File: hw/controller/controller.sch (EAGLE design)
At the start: 74 parts, among them J1 JST-PH3SMT_VERT, J2 JST-PH3SMT_VERT, Q1 TPN1R603PL, Q2 TPN1R603PL, Q3 TPN1R603PL, Q4 TPN1R603PL, Q5 TPN1R603PL, Q6 TPN1R603PL, U1 STM32F4R_64PIN, U2 DRV8323RS, U3 AS5147, U4 MAX13431E, X1 8.0MHz

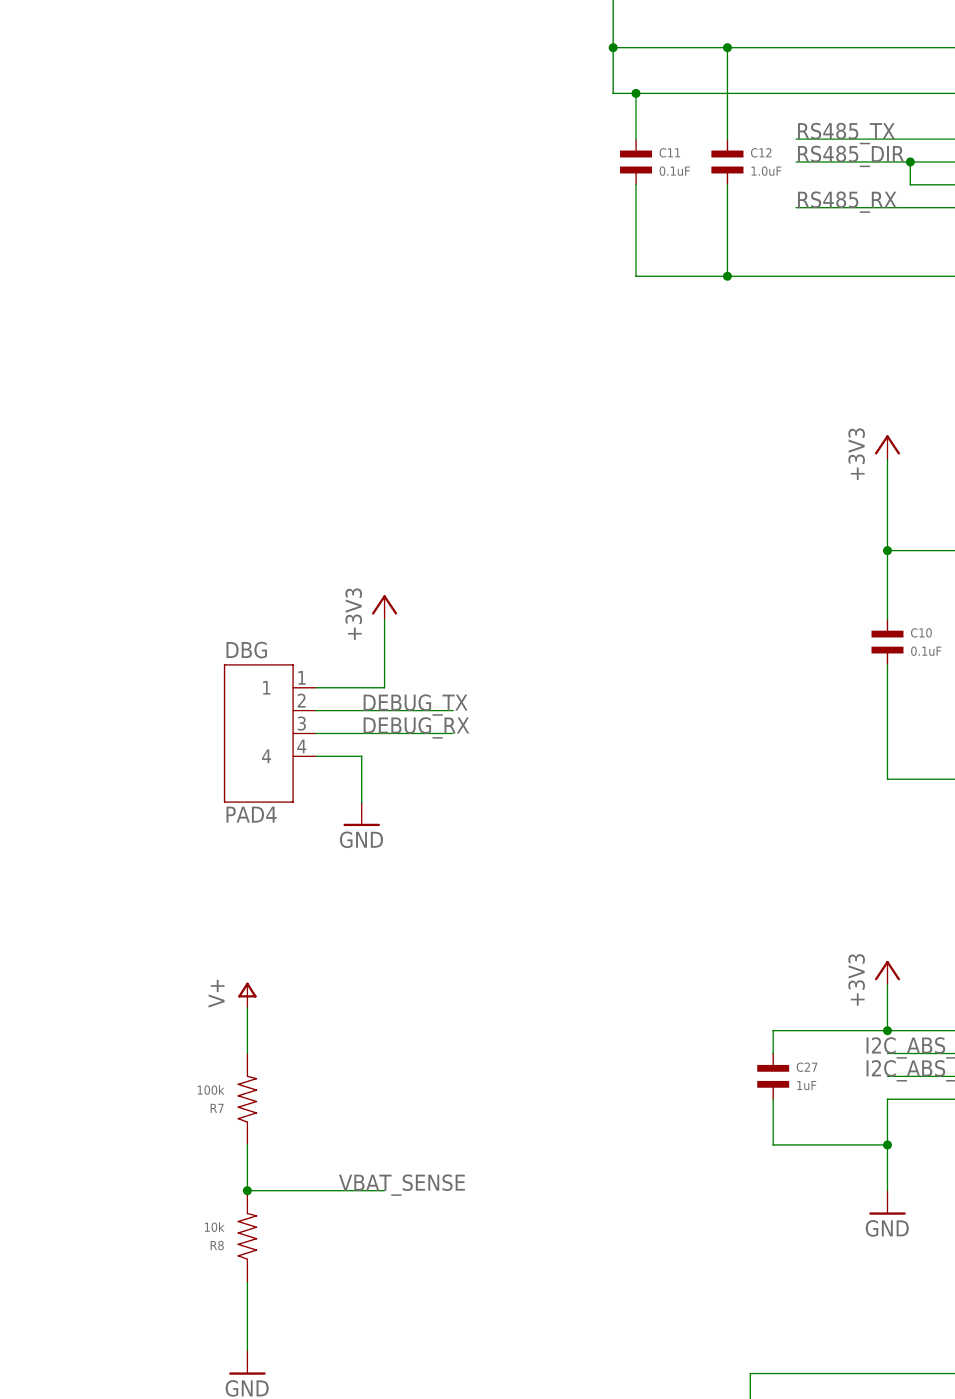
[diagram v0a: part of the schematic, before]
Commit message: More BOM tweaks
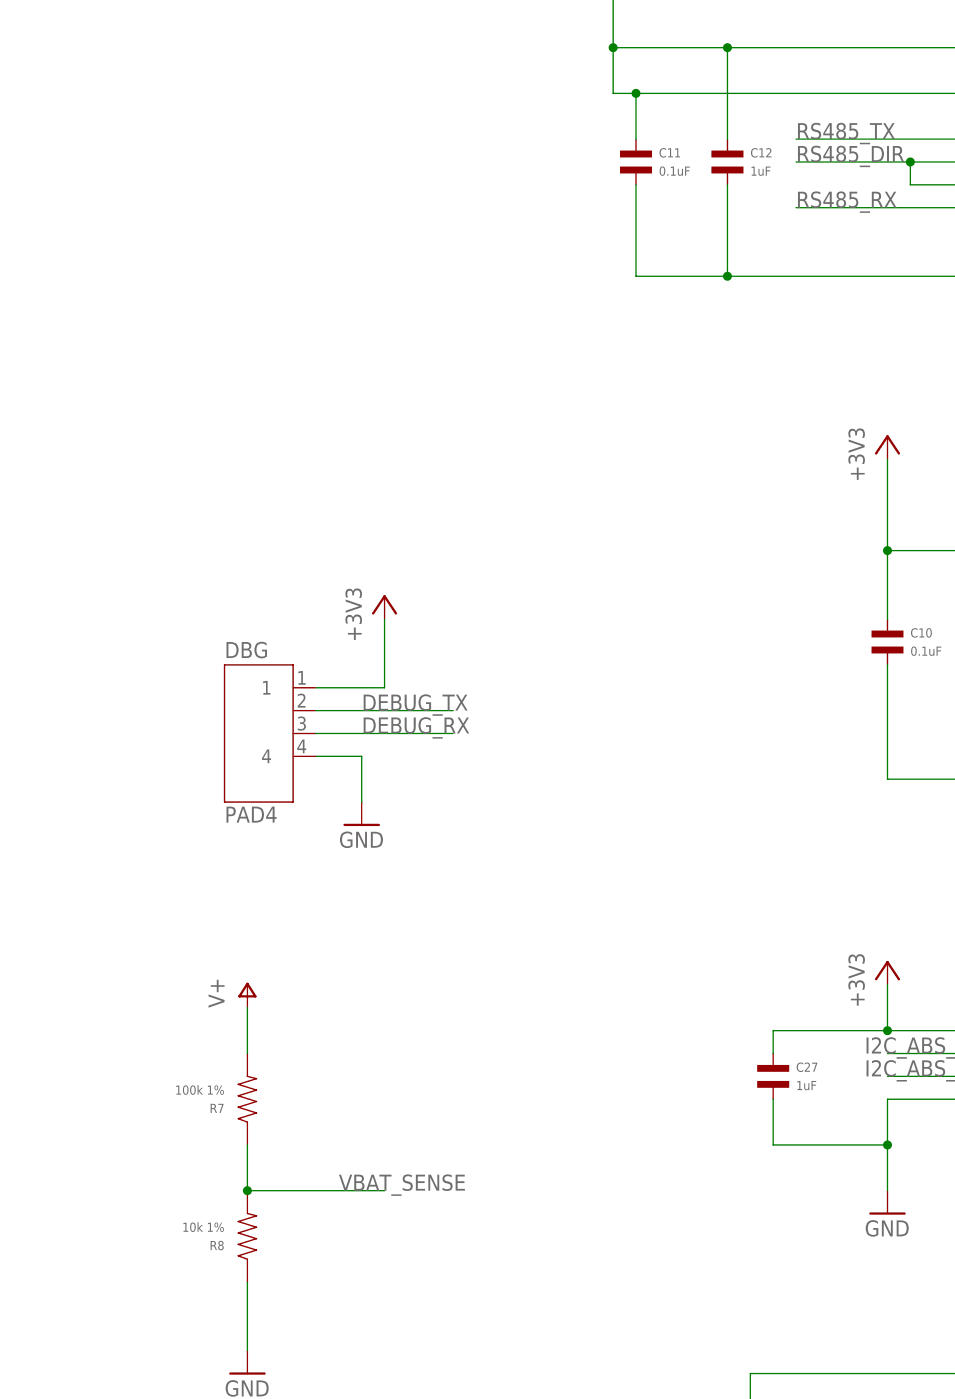
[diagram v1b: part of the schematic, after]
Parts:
- C12: value 1.0uF -> 1uF; MPN MF-CAP-0402-0.1uF -> MF-CAP-0402-1uF
- R4: MPN P10.0KHCT-ND -> ERJ-3EKF1002V
- R7: value 100k -> 100k 1%
- R8: value 10k -> 10k 1%
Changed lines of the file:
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@@
 </part>
 <part name="GND18" library="supply1" deviceset="GND" device=""/>
-<part name="R7" library="mfpassives" deviceset="RESISTOR" device="_0603" value="100k">
+<part name="R7" library="mfpassives" deviceset="RESISTOR" device="_0603" value="100k 1%">
 <attribute name="DPN" value="P100KHCT-ND"/>
 <attribute name="MPN" value="ERJ-3EKF1003V"/>
 </part>
-<part name="R8" library="mfpassives" deviceset="RESISTOR" device="_0603" value="10k">
+<part name="R8" library="mfpassives" deviceset="RESISTOR" device="_0603" value="10k 1%">
 <attribute name="DPN" value="P10.0KHCT-ND"/>
 <attribute name="MPN" value="ERJ-3EKF1002V"/>
@@
 <attribute name="MPN" value="MF-CAP-0402-0.1uF"/>
 </part>
-<part name="C12" library="mfpassives" deviceset="CAPACITOR_NP" device="_0402" value="1.0uF">
+<part name="C12" library="mfpassives" deviceset="CAPACITOR_NP" device="_0402" value="1uF">
 <attribute name="HOUSEPART" value="1"/>
-<attribute name="MPN" value="MF-CAP-0402-0.1uF"/>
+<attribute name="MPN" value="MF-CAP-0402-1uF"/>
 </part>
 <part name="RA" library="rcl" deviceset="R-US_" device="M1206" value="1mOhm 1% 2W">
@@
 <part name="R4" library="mfpassives" deviceset="RESISTOR" device="_0603" value="10k 1%">
 <attribute name="MF" value="Panasonic"/>
-<attribute name="MPN" value="P10.0KHCT-ND"/>
+<attribute name="MPN" value="ERJ-3EKF1002V"/>
 </part>
 <part name="GND7" library="supply1" deviceset="GND" device=""/>

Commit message: MF doesn't have a 0402 10pF cap
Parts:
- C8, C9: HOUSEPART 1 -> (none); MF (none) -> Samsung Electro-Mechanics; MPN MF-CAP-0402-10pF -> CL05C100JB51PNC
- R8: DPN P10.0KHCT-ND -> (none); MF (none) -> Panasonic
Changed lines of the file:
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@@
 <part name="GND17" library="supply1" deviceset="GND" device=""/>
 <part name="C8" library="mfpassives" deviceset="CAPACITOR_NP" device="_0402" value="10pF">
-<attribute name="HOUSEPART" value="1"/>
-<attribute name="MPN" value="MF-CAP-0402-10pF"/>
+<attribute name="MF" value="Samsung Electro-Mechanics"/>
+<attribute name="MPN" value="CL05C100JB51PNC"/>
 </part>
 <part name="C9" library="mfpassives" deviceset="CAPACITOR_NP" device="_0402" value="10pF">
-<attribute name="HOUSEPART" value="1"/>
-<attribute name="MPN" value="MF-CAP-0402-10pF"/>
+<attribute name="MF" value="Samsung Electro-Mechanics"/>
+<attribute name="MPN" value="CL05C100JB51PNC"/>
 </part>
 <part name="GND18" library="supply1" deviceset="GND" device=""/>
@@
 </part>
 <part name="R8" library="mfpassives" deviceset="RESISTOR" device="_0603" value="10k 1%">
-<attribute name="DPN" value="P10.0KHCT-ND"/>
+<attribute name="MF" value="Panasonic"/>
 <attribute name="MPN" value="ERJ-3EKF1002V"/>
 </part>
@@
 <instance part="C8" gate="G$1" x="182.88" y="7.62">
 <attribute name="MPN" x="182.88" y="7.62" size="1.778" layer="96" display="off"/>
+<attribute name="MF" x="182.88" y="7.62" size="1.778" layer="96" display="off"/>
 </instance>
 <instance part="C9" gate="G$1" x="223.52" y="7.62">
 <attribute name="MPN" x="223.52" y="7.62" size="1.778" layer="96" display="off"/>
+<attribute name="MF" x="223.52" y="7.62" size="1.778" layer="96" display="off"/>
 </instance>
 <instance part="GND18" gate="1" x="-5.08" y="-218.44"/>
@@
 </instance>
 <instance part="R8" gate="G$1" x="-5.08" y="-203.2" rot="R180">
-<attribute name="DPN" x="-5.08" y="-203.2" size="1.778" layer="96" rot="R180" display="off"/>
 <attribute name="MPN" x="-5.08" y="-203.2" size="1.778" layer="96" rot="R180" display="off"/>
+<attribute name="MF" x="-5.08" y="-203.2" size="1.778" layer="96" rot="R180" display="off"/>
 </instance>
 <instance part="GND6" gate="1" x="88.9" y="-45.72"/>

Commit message: Reduce unique part count to 21
 * Subbed in more expensive parts where cheaper ones would do
 * Changed a few resistor/capacitor values to things that are "close
   enough"
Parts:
- C10, C11, C2, C26, C3, C4, C5, C6: value 0.1uF -> 0.1uF 50V; HOUSEPART 1 -> (none); MF (none) -> TDK; MPN MF-CAP-0402-0.1uF -> C1005X7R1H104K050BE
- C12, C24, C25, C27: value 1uF -> 1uF 35V; HOUSEPART 1 -> (none); MF (none) -> Samsung Electro-Mechanics; MPN MF-CAP-0402-1uF -> CL05A105KL5NRNC
- C14, C15, C16, C17, C18, C19: device rcl:C-USC1206 -> mfpassives:CAPACITOR_NP_1206; POPULATE 1 -> (none)
- C20: value 10uF -> 15uF; HOUSEPART 1 -> (none); MF (none) -> TDK; MPN MF-CAP-1206-10uF -> C3216X5R1V156M160AC
- C22: value 47nF 35V -> 0.1uF 50V; device mfpassives:CAPACITOR_NP_0603 -> mfpassives:CAPACITOR_NP_0402; MPN CGA2B3X5R1V473K050BB -> C1005X7R1H104K050BE
- D2: value MF-LED-0603-GREEN -> MF-LED-0603-RED; device mfleds:LED_SINGLE-0603-GREEN -> mfleds:LED_SINGLE-0603-RED
- R1: value 10 -> 220; MPN MF-RES-0402-10 -> MF-RES-0402-220
- R2: value 100k -> 100k 1%; HOUSEPART 1 -> (none); MF (none) -> Panasonic; MPN MF-RES-0402-100K -> ERJ-2RKF1003X
- R3: device mfpassives:RESISTOR_0603 -> mfpassives:RESISTOR_0402; MPN ERJ-3EKF3322V -> ERJ-2RKF3322X
- R4, R8: device mfpassives:RESISTOR_0603 -> mfpassives:RESISTOR_0402; MPN ERJ-3EKF1002V -> ERJ-2RKF1002X
- R5: value 10k -> 10k 1%; HOUSEPART 1 -> (none); MF (none) -> Panasonic; MPN MF-RES-0402-10K -> ERJ-2RKF1002X
- R7: device mfpassives:RESISTOR_0603 -> mfpassives:RESISTOR_0402; DPN P100KHCT-ND -> (none); MF (none) -> Panasonic; MPN ERJ-3EKF1003V -> ERJ-2RKF1003X
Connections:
- net V+: now also C14.P$1, C15.P$1, C16.P$1, C17.P$1, C18.P$1, C19.P$1; no longer C14.1, C15.1, C16.1, C17.1, C18.1, C19.1
- net V-: now also C14.P$2, C15.P$2, C16.P$2, C17.P$2, C18.P$2, C19.P$2; no longer C14.2, C15.2, C16.2, C17.2, C18.2, C19.2

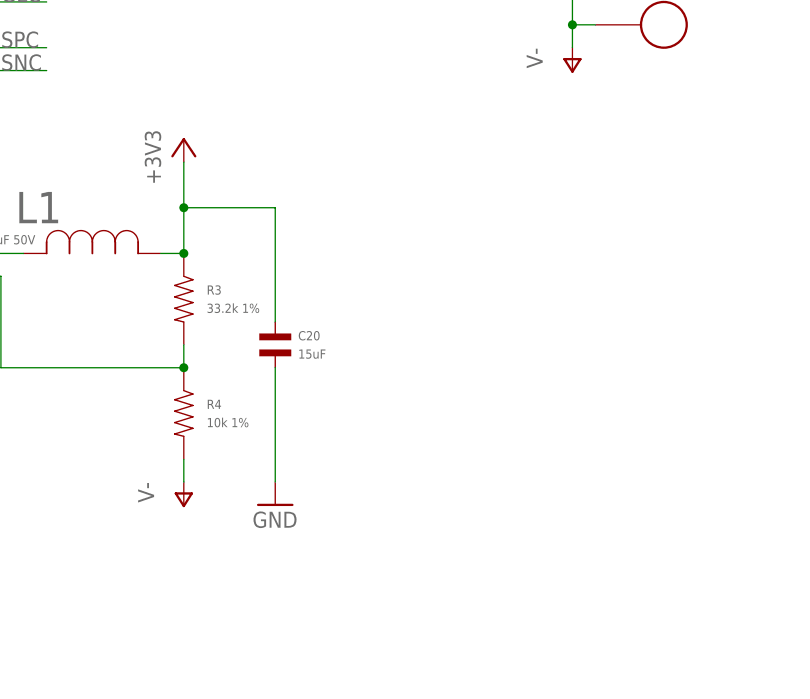
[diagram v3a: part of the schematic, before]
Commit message: Down to 20!  * Swapped in 3x 100k resistors for the 33.2k
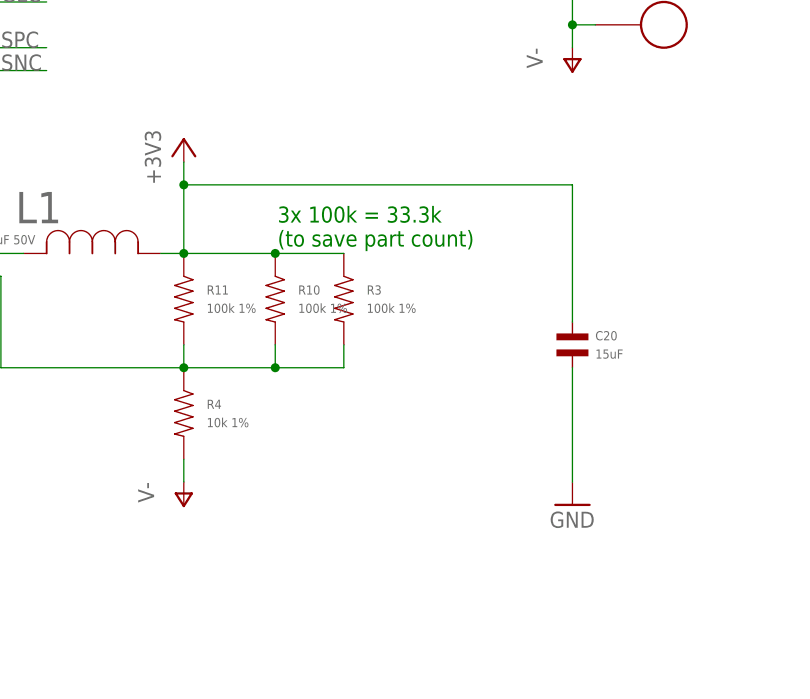
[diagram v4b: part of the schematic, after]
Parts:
- added R10, R11: 100k 1%, mfpassives:RESISTOR_0402
- R3: value 33.2k 1% -> 100k 1%; MPN ERJ-2RKF3322X -> ERJ-2RKF1003X
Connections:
- net +3V3: now also R10.P$1, R11.P$1
- net N$8: now also R10.P$2, R11.P$2
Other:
- note added: "3x 100k = 33.3k (to save part count)"
- moved on the sheet: C20, R3
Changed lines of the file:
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@@
 </part>
 <part name="+3V3" library="supply1" deviceset="+3V3" device=""/>
-<part name="R3" library="mfpassives" deviceset="RESISTOR" device="_0402" value="33.2k 1%">
-<attribute name="MF" value="Panasonic"/>
-<attribute name="MPN" value="ERJ-2RKF3322X"/>
-</part>
 <part name="R4" library="mfpassives" deviceset="RESISTOR" device="_0402" value="10k 1%">
 <attribute name="MF" value="Panasonic"/>
@@
 <attribute name="MPN" value="C3216X5R1V156M160AC"/>
 </part>
+<part name="R3" library="mfpassives" deviceset="RESISTOR" device="_0402" value="100k 1%">
+<attribute name="MF" value="Panasonic"/>
+<attribute name="MPN" value="ERJ-2RKF1003X"/>
+</part>
+<part name="R10" library="mfpassives" deviceset="RESISTOR" device="_0402" value="100k 1%">
+<attribute name="MF" value="Panasonic"/>
+<attribute name="MPN" value="ERJ-2RKF1003X"/>
+</part>
+<part name="R11" library="mfpassives" deviceset="RESISTOR" device="_0402" value="100k 1%">
+<attribute name="MF" value="Panasonic"/>
+<attribute name="MPN" value="ERJ-2RKF1003X"/>
+</part>
 </parts>
 <sheets>
 <sheet>
 <plain>
+<text x="145.034" y="-324.358" size="1.778" layer="91">3x 100k = 33.3k
+(to save part count)</text>
 </plain>
 <instances>
@@
 </instance>
 <instance part="+3V3" gate="G$1" x="134.62" y="-312.42"/>
-<instance part="R3" gate="G$1" x="134.62" y="-330.2">
-<attribute name="MPN" x="134.62" y="-330.2" size="1.778" layer="96" display="off"/>
-<attribute name="MF" x="134.62" y="-330.2" size="1.778" layer="96" display="off"/>
-</instance>
 <instance part="R4" gate="G$1" x="134.62" y="-342.9">
 <attribute name="MPN" x="134.62" y="-342.9" size="1.778" layer="96" display="off"/>
 <attribute name="MF" x="134.62" y="-342.9" size="1.778" layer="96" display="off"/>
 </instance>
-<instance part="GND7" gate="1" x="144.78" y="-353.06"/>
+<instance part="GND7" gate="1" x="177.8" y="-353.06"/>
 <instance part="C21" gate="G$1" x="109.22" y="-322.58">
 <attribute name="MPN" x="109.22" y="-322.58" size="1.778" layer="96" display="off"/>
@@
 </instance>
 <instance part="P-8" gate="1" x="25.4" y="-340.36"/>
-<instance part="C20" gate="G$1" x="144.78" y="-335.28">
-<attribute name="MF" x="144.78" y="-335.28" size="1.778" layer="96" display="off"/>
+<instance part="C20" gate="G$1" x="177.8" y="-335.28">
+<attribute name="MF" x="177.8" y="-335.28" size="1.778" layer="96" display="off"/>
 </instance>
 <instance part="C14" gate="G$1" x="264.16" y="-210.82">
@@
 <instance part="C19" gate="G$1" x="233.68" y="-210.82">
 <attribute name="MF" x="233.68" y="-210.82" size="1.778" layer="96" display="off"/>
+</instance>
+<instance part="R3" gate="G$1" x="152.4" y="-330.2">
+<attribute name="MPN" x="152.4" y="-330.2" size="1.778" layer="96" display="off"/>
+<attribute name="MF" x="152.4" y="-330.2" size="1.778" layer="96" display="off"/>
+</instance>
+<instance part="R10" gate="G$1" x="144.78" y="-330.2">
+<attribute name="MPN" x="144.78" y="-330.2" size="1.778" layer="96" display="off"/>
+<attribute name="MF" x="144.78" y="-330.2" size="1.778" layer="96" display="off"/>
+</instance>
+<instance part="R11" gate="G$1" x="134.62" y="-330.2">
+<attribute name="MPN" x="134.62" y="-330.2" size="1.778" layer="96" display="off"/>
+<attribute name="MF" x="134.62" y="-330.2" size="1.778" layer="96" display="off"/>
 </instance>
 </instances>
@@
 </segment>
 <segment>
-<pinref part="R3" gate="G$1" pin="P$1"/>
 <pinref part="+3V3" gate="G$1" pin="+3V3"/>
-<wire x1="134.62" y1="-325.12" x2="134.62" y2="-320.04" width="0.1524" layer="91"/>
-<wire x1="134.62" y1="-320.04" x2="134.62" y2="-314.96" width="0.1524" layer="91"/>
-<wire x1="144.78" y1="-332.74" x2="144.78" y2="-320.04" width="0.1524" layer="91"/>
-<wire x1="144.78" y1="-320.04" x2="134.62" y2="-320.04" width="0.1524" layer="91"/>
-<junction x="134.62" y="-320.04"/>
+<wire x1="134.62" y1="-325.12" x2="134.62" y2="-317.5" width="0.1524" layer="91"/>
+<wire x1="134.62" y1="-317.5" x2="134.62" y2="-314.96" width="0.1524" layer="91"/>
+<wire x1="177.8" y1="-332.74" x2="177.8" y2="-317.5" width="0.1524" layer="91"/>
+<wire x1="177.8" y1="-317.5" x2="134.62" y2="-317.5" width="0.1524" layer="91"/>
+<junction x="134.62" y="-317.5"/>
 <pinref part="L1" gate="A" pin="1"/>
 <wire x1="132.08" y1="-325.12" x2="134.62" y2="-325.12" width="0.1524" layer="91"/>
+<pinref part="C20" gate="G$1" pin="P$1"/>
+<pinref part="R11" gate="G$1" pin="P$1"/>
 <junction x="134.62" y="-325.12"/>
-<pinref part="C20" gate="G$1" pin="P$1"/>
+<pinref part="R10" gate="G$1" pin="P$1"/>
+<wire x1="134.62" y1="-325.12" x2="144.78" y2="-325.12" width="0.1524" layer="91"/>
+<pinref part="R3" gate="G$1" pin="P$1"/>
+<wire x1="144.78" y1="-325.12" x2="152.4" y2="-325.12" width="0.1524" layer="91"/>
+<junction x="144.78" y="-325.12"/>
 </segment>
 <segment>
@@
 </segment>
 <segment>
-<wire x1="144.78" y1="-350.52" x2="144.78" y2="-337.82" width="0.1524" layer="91"/>
+<wire x1="177.8" y1="-350.52" x2="177.8" y2="-337.82" width="0.1524" layer="91"/>
 <pinref part="GND7" gate="1" pin="GND"/>
 <pinref part="C20" gate="G$1" pin="P$2"/>
@@
 <segment>
 <pinref part="R4" gate="G$1" pin="P$1"/>
-<pinref part="R3" gate="G$1" pin="P$2"/>
 <wire x1="134.62" y1="-337.82" x2="134.62" y2="-335.28" width="0.1524" layer="91"/>
 <pinref part="U2" gate="G$1" pin="FB"/>
@@
 <wire x1="114.3" y1="-337.82" x2="134.62" y2="-337.82" width="0.1524" layer="91"/>
 <junction x="134.62" y="-337.82"/>
-</segment>
-</net>
+<pinref part="R11" gate="G$1" pin="P$2"/>
+<pinref part="R10" gate="G$1" pin="P$2"/>
+<wire x1="134.62" y1="-337.82" x2="144.78" y2="-337.82" width="0.1524" layer="91"/>
+<wire x1="144.78" y1="-337.82" x2="144.78" y2="-335.28" width="0.1524" layer="91"/>
+<pinref part="R3" gate="G$1" pin="P$2"/>
+<wire x1="144.78" y1="-337.82" x2="152.4" y2="-337.82" width="0.1524" layer="91"/>
+<wire x1="152.4" y1="-337.82" x2="152.4" y2="-335.28" width="0.1524" layer="91"/>
+<junction x="144.78" y="-337.82"/>
+</segment>
+</net>
